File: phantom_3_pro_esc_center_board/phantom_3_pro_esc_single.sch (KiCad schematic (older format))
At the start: 103 parts, among them M2 Brushless_Motor_3phase, Q10 AON6504, Q11 AON6504, Q12 AON6504, Q7 AON6504, Q8 AON6504, Q9 AON6504, T2 TMS320F28027F, Y3 ?MHz, Y4 ?MHz

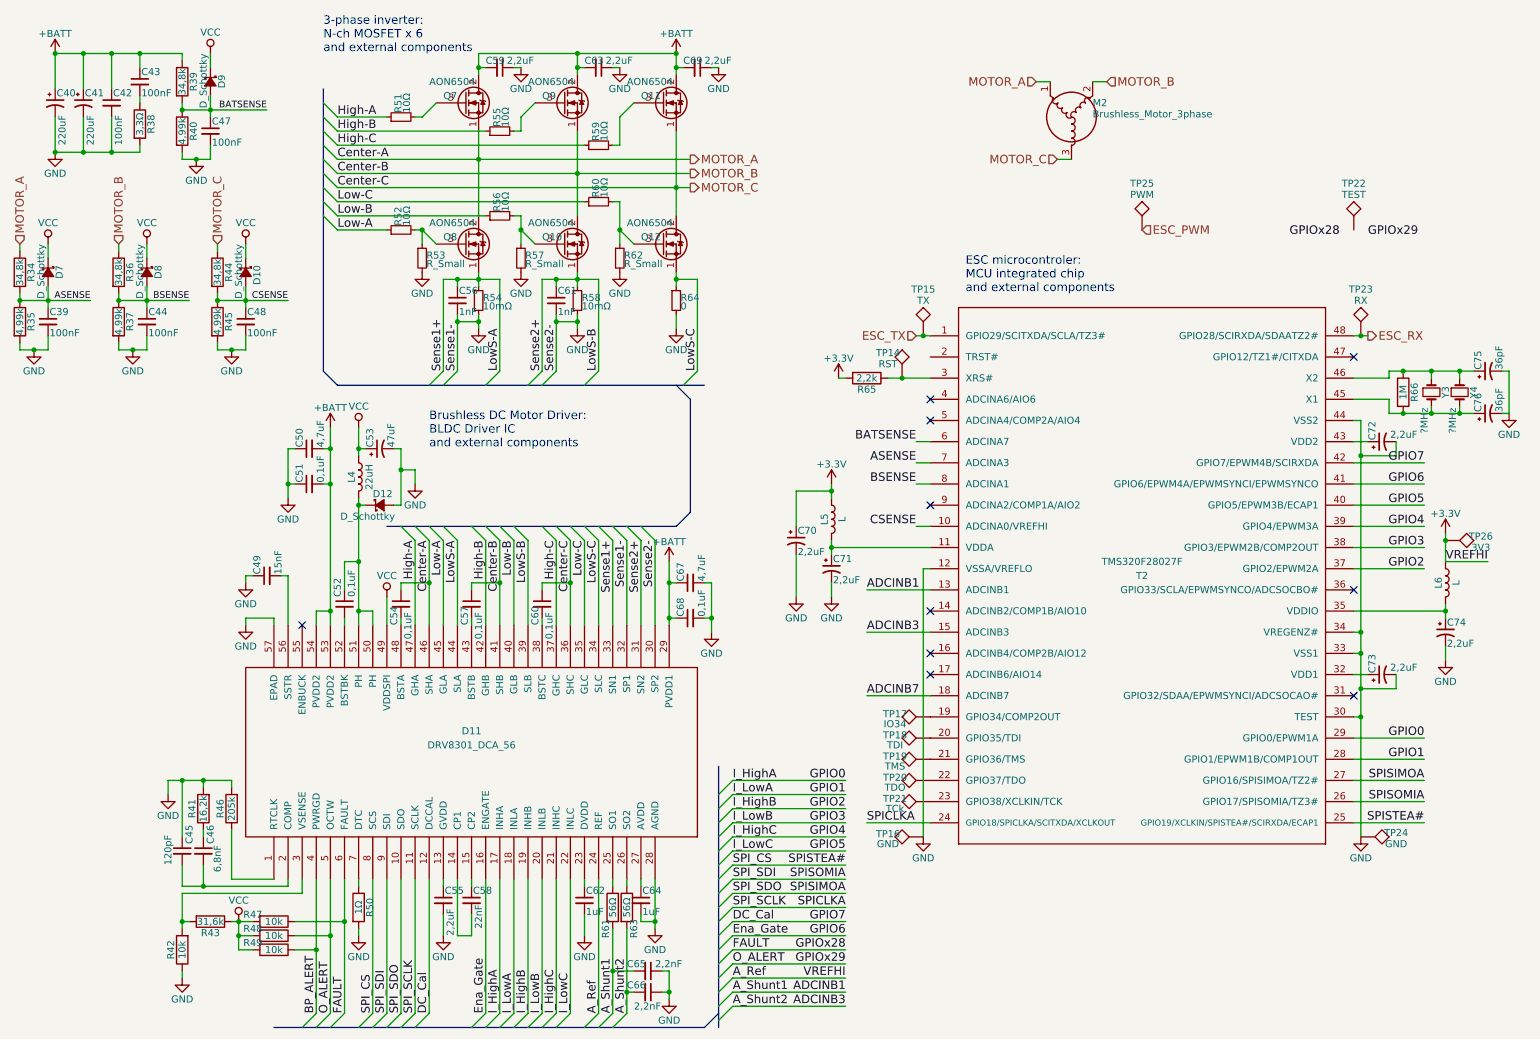
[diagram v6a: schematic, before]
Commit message: ESC Center: Formed a link between schematic and PCB.
Modified PCB to link some components to schematic.

Also created edge pad connectors to FC board.
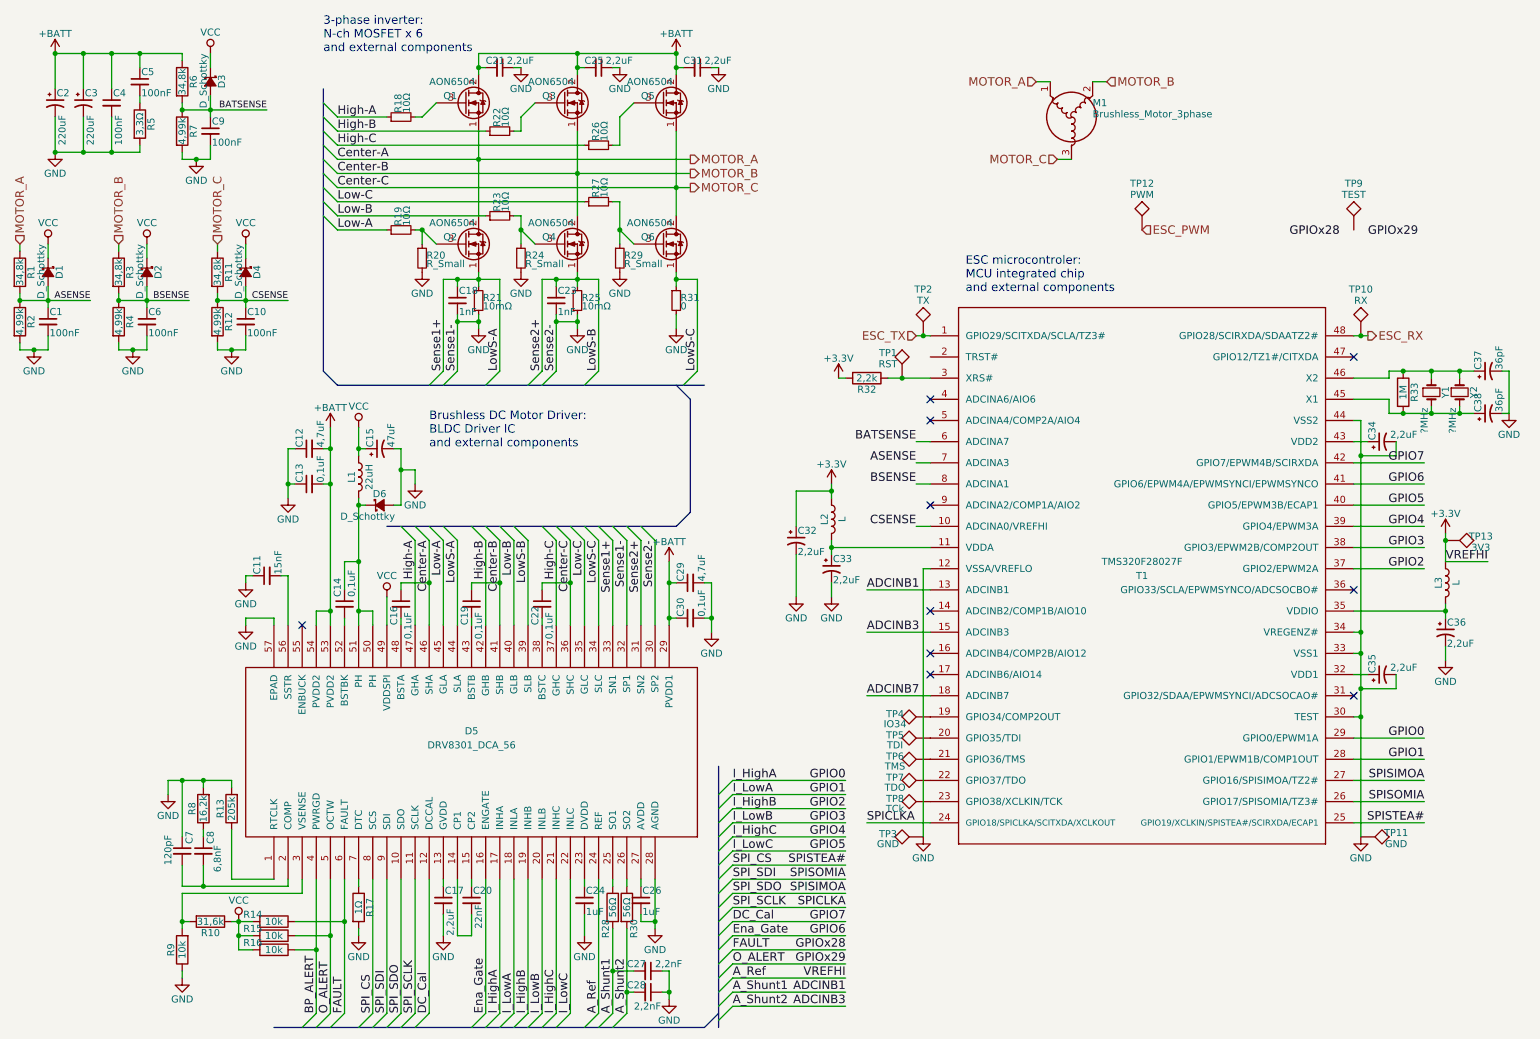
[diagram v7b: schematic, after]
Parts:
- C39, C40, C41, C42, C43, C44, C45, C46, C47, C48, C49, C50, C51, C52, C53, C54, C55, C56, C57, C58, C59, C60, C61, C62, C63, C64, C65, C66, C67, C68, C69, C70, C71, C72, C73, C74, C75, C76: footprint (none) -> Capacitors_SMD:C_0201

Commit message: All: Preparing for KiCad version change.
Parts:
- TP14, TP15, TP16, TP17, TP18, TP19, TP20, TP21, TP22, TP23, TP24, TP25, TP26: symbol TEST -> Connector:TestPoint
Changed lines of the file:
@@
 ESC_TX
 $Comp
-L TEST TP20
+L Connector:TestPoint TP20
 U 1 1 590A42AE
 P 7000 5950
@@
 $EndComp
 $Comp
-L TEST TP18
+L Connector:TestPoint TP18
 U 1 1 590A6EE9
 P 7000 5650
@@
 $EndComp
 $Comp
-L TEST TP19
+L Connector:TestPoint TP19
 U 1 1 590A6EEF
 P 7000 5800
@@
 $EndComp
 $Comp
-L TEST TP21
+L Connector:TestPoint TP21
 U 1 1 590A6EF5
 P 7000 6100
@@
 $EndComp
 $Comp
-L TEST TP17
+L Connector:TestPoint TP17
 U 1 1 590A6EFB
 P 7000 5500
@@
 $EndComp
 $Comp
-L TEST TP15
+L Connector:TestPoint TP15
 U 1 1 590A73EC
 P 6950 2800
@@
 $EndComp
 $Comp
-L TEST TP22
+L Connector:TestPoint TP22
 U 1 1 590A73F2
 P 10000 2050
@@
 $EndComp
 $Comp
-L TEST TP14
+L Connector:TestPoint TP14
 U 1 1 590A73F8
 P 6800 3100
@@
 $EndComp
 $Comp
-L TEST TP25
+L Connector:TestPoint TP25
 U 1 1 590A73FE
 P 8500 2050
@@
 $EndComp
 $Comp
-L TEST TP26
+L Connector:TestPoint TP26
 U 1 1 590A7404
 P 10650 4250
@@
 $EndComp
 $Comp
-L TEST TP16
+L Connector:TestPoint TP16
 U 1 1 590A740A
 P 6950 6350
@@
 $EndComp
 $Comp
-L TEST TP24
+L Connector:TestPoint TP24
 U 1 1 590A7410
 P 10050 6350
@@
 $EndComp
 $Comp
-L TEST TP23
+L Connector:TestPoint TP23
 U 1 1 590A7416
 P 10050 2800
